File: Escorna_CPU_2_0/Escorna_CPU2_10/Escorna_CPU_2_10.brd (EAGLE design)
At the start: 49.9 x 89.6 mm, 84 parts, among them IC1 ULN2803, U2 ESP01, X1 AK550/2, X1.1 AK550/2

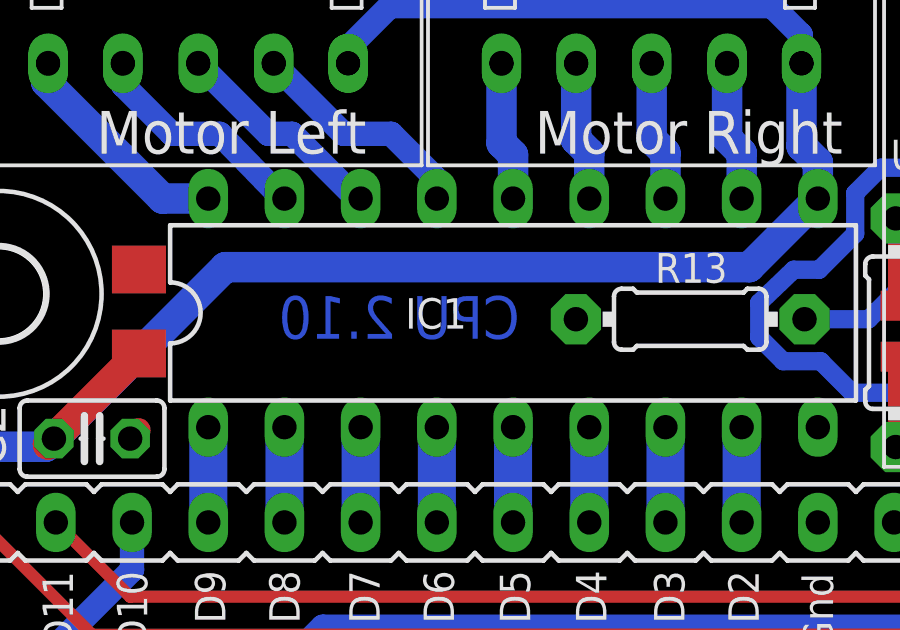
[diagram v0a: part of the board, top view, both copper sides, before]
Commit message: new values
New values of resistors, (R5) for the switch S5 and (R10) improves the
brightness of the green LED.
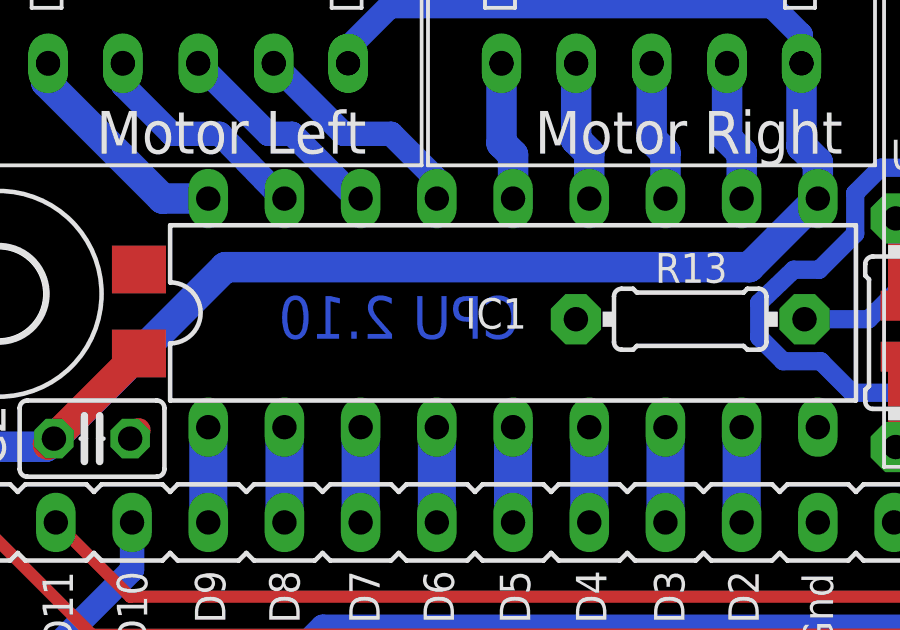
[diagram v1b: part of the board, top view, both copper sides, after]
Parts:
- R10, R10.1: value 1K -> 100
- R5, R5.1: value 10K -> 22K
- renumbered S1.2 to S2.1, S1.3 to S3.1, S1.4 to S4.1, S1.5 to S5.1
